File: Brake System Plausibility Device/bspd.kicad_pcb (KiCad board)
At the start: 2 copper layers, 87.9 x 41.3 mm, 29 parts, among them P1 MX150_16, SW1 RESET, U1 MCP604, U2 LM1117-5.0, U3 74LVC2G74, U4 74AUC2G00

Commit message: BSPD Layout Done
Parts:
- removed P1: MX150_16, UNCAMotorsports:MX150_16pin
- removed R12, R13: 1k, Resistors_SMD:R_0805_HandSoldering
- removed RV1: 5KW trim - 10k, Potentiometers:Potentiometer_Trimmer_Bourns_3296W
- removed RV2: Braking trim - 10k, Potentiometers:Potentiometer_Trimmer_Bourns_3296W
- added BR: BRAKE_SENSOR, Pin_Headers:Pin_Header_Straight_1x03_Pitch2.54mm, F.Cu at (133.0, 88.8)
- added B_TR: 5KW trim - 10k, Potentiometers:Potentiometer_Trimmer_Bourns_3296W, F.Cu at (123.3, 105.2)
- added C5: 1u, Capacitors_SMD:C_0805_HandSoldering, B.Cu at (116.2, 98.4)
- added C6: 1u, Capacitors_SMD:C_0805_HandSoldering, F.Cu at (131.4, 101.1)
- added C7: 1u, Capacitors_SMD:C_0805_HandSoldering, B.Cu at (128.8, 106.9)
- added I_SNS_1: CURRENT_SENSE_2, Pin_Headers:Pin_Header_Straight_1x03_Pitch2.54mm, F.Cu at (110.2, 88.9)
- added I_SNS_2: CURRENT_SENSE_1, Pin_Headers:Pin_Header_Straight_1x03_Pitch2.54mm, F.Cu at (110.2, 101.3)
- added I_TR: Braking trim - 10k, Potentiometers:Potentiometer_Trimmer_Bourns_3296W, F.Cu at (123.3, 89.7)
- added OUT: Q_QNOT_LATCHED, Pin_Headers:Pin_Header_Straight_1x02_Pitch2.54mm, F.Cu at (137.0, 106.4)
- added PWR: 12V_AND_GND, Pin_Headers:Pin_Header_Straight_1x02_Pitch2.54mm, F.Cu at (144.4, 98.3)
- added REF**: MountingHole_3.2mm_M3, Mounting_Holes:MountingHole_3.2mm_M3, F.Cu at (104.9, 104.8)
- added REF**: MountingHole_3.2mm_M3, Mounting_Holes:MountingHole_3.2mm_M3, F.Cu at (104.9, 90.4)
- added REF**: MountingHole_3.2mm_M3, Mounting_Holes:MountingHole_3.2mm_M3, F.Cu at (149.9, 104.8)
- added REF**: MountingHole_3.2mm_M3, Mounting_Holes:MountingHole_3.2mm_M3, F.Cu at (149.9, 90.4)
- C1, C2, D1, D2, D3, F1, R3, R4, R8, R9: moved to B.Cu
- C3: footprint Capacitors_ThroughHole:CP_Radial_D5.0mm_P2.00mm -> Capacitors_ThroughHole:CP_Radial_D6.3mm_P2.50mm
- R11: value 1k -> 10k
- SW1: value RESET -> SW_Push; footprint Buttons_Switches_ThroughHole:SW_PUSH_6mm -> Pin_Headers:Pin_Header_Straight_1x02_Pitch2.54mm
- U1: footprint Housings_SSOP:TSSOP-14_4.4x5mm_Pitch0.65mm -> SMD_Packages:SSOP-14
- U3: footprint Housings_SSOP:TSSOP-8_3x3mm_Pitch0.65mm -> Housings_SSOP:VSSOP-8_2.3x2mm_Pitch0.5mm
- moved R6 72.6 mm to (118.2, 94.1), turned to 180 degrees
- moved D2 69.5 mm to (125.1, 100.8), turned to 180 degrees
- moved C3 67.9 mm to (128.4, 94.7)
- moved U1 65.9 mm to (116.2, 98.5), turned to 270 degrees
- moved D1 61.3 mm to (120.2, 94.1), turned to 180 degrees
- moved C2 60.2 mm to (140.3, 91.7), turned to 270 degrees
- moved U2 58.4 mm to (139.6, 90.7), turned to 180 degrees
- moved U4 56.0 mm to (128.8, 105.7)
- moved SW1 55.5 mm to (142.0, 106.3), turned to 90 degrees
- moved C1 54.3 mm to (139.1, 88.4), turned to 180 degrees
- moved U3 46.5 mm to (128.0, 101.1), turned to 90 degrees
- moved C4 44.9 mm to (135.5, 97.5)
- moved R2 44.6 mm to (113.3, 104.0), turned to 270 degrees
- moved R7 42.8 mm to (122.9, 97.5), turned to 180 degrees
- moved R4 41.4 mm to (113.3, 105.4), turned to 270 degrees
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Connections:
- R11 pad 1: GND -> Net-(R11-Pad1)
- R11 pad 2: Net-(R11-Pad2) -> +5V
- SW1 pad 1: Net-(R11-Pad2) -> Net-(R11-Pad1)
- SW1 pad 2: +5V -> GND
- U3 pad 3: Net-(R13-Pad2) -> /BSPD_Latched_Output_NOT
- U3 pad 5: /TO_BTS6133 -> /BSPD_Latched_Output
- U4 pad 2: Net-(R11-Pad2) -> Net-(U4-Pad2)
- U4 pad 3: (no net) -> Net-(U4-Pad2)
- U4 pad 5: GND -> Net-(R11-Pad1)
- U4 pad 6: GND -> Net-(R11-Pad1)
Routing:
- net +5V: track 0.00 -> 45.6 mm, vias 0 -> 7
- net +12V: track 44.1 -> 5.53 mm, vias 0 -> 1
- net GND: track 0.00 -> 33.4 mm, vias 0 -> 6
- net /BSPD_Latched_Output: track 0.00 -> 25.5 mm, vias 0 -> 4
- net /BSPD: track 0.00 -> 20.8 mm, vias 0 -> 3
- net /Hard_Braking: track 0.00 -> 17.7 mm, vias 0 -> 4
- net Net-(R11-Pad1): track 0.00 -> 16.1 mm, vias 0 -> 2
- net Net-(R1-Pad2): track 0.00 -> 14.8 mm, vias 0 -> 2
- net Net-(C4-Pad1): track 0.00 -> 12.5 mm, vias 0 -> 2
- net Net-(C1-Pad1): track 0.00 -> 10.6 mm, vias 0 -> 1
- net /Current_R: track 0.00 -> 9.69 mm, vias 0 -> 2
- net Net-(RV2-Pad2): track 0.00 -> 9.45 mm
- net Net-(R10-Pad1): track 0.00 -> 8.46 mm
- net /BSPD_Latched_Output_NOT: track 0.00 -> 8.36 mm, vias 0 -> 1
- net Net-(D2-Pad2): track 0.00 -> 8.35 mm, vias 0 -> 2
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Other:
- board size 87.9 x 41.3 mm -> 52.1 x 21.5 mm
- net class Default: clearance 0.254 -> 0.1524
- rule trace_clearance: 0.254 -> 0.1524

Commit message: Fixed board error on BSPD
Track near via error corrected
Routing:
- net GND: vias 6 -> 5
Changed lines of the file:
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@@
 (kicad_pcb (version 4) (host pcbnew 4.0.6)
   (general
-    (links 0)
-    (no_connects 22)
-    (area 101.270999 86.792999 153.491001 108.406001)
+    (links 77)
+    (no_connects 0)
+    (area 95.392457 85.1786 159.369543 113.006972)
     (thickness 1.6)
     (drawings 12)
-    (tracks 255)
+    (tracks 254)
     (zones 0)
     (modules 38)
@@
     (pad_to_mask_clearance 0.2)
     (aux_axis_origin 0 0)
-    (visible_elements 7FFFFFFF)
+    (visible_elements 7FFFEFFF)
     (pcbplotparams
       (layerselection 0x00030_80000001)
@@
   (segment (start 128.762 102.854782) (end 128.928655 103.021437) (width 0.254) (layer F.Cu) (net 2))
   (segment (start 128.762 102.642) (end 128.762 102.854782) (width 0.254) (layer F.Cu) (net 2))
-  (via (at 129.413588 103.021437) (size 0.6858) (drill 0.3302) (layers F.Cu B.Cu) (net 2))
   (segment (start 128.928655 103.021437) (end 129.413588 103.021437) (width 0.254) (layer F.Cu) (net 2))
   (segment (start 129.413588 102.805613) (end 129.413588 103.021437) (width 0.254) (layer F.Cu) (net 2))

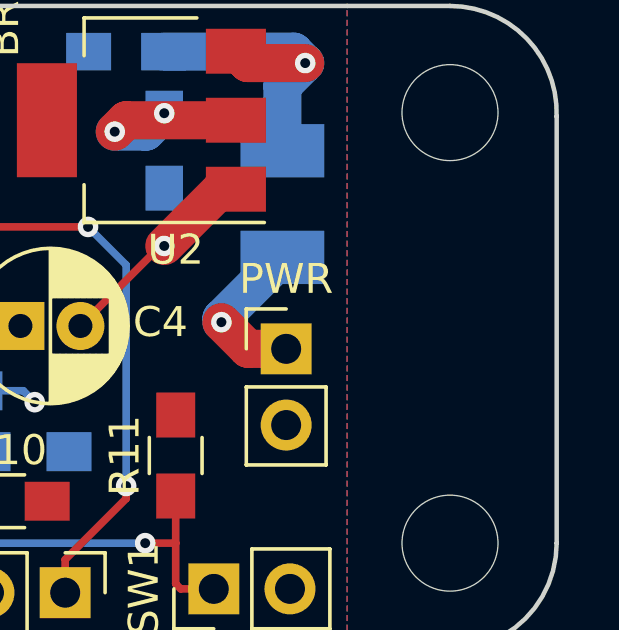
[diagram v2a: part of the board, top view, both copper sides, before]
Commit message: Reduce pour clearance to .1", add label
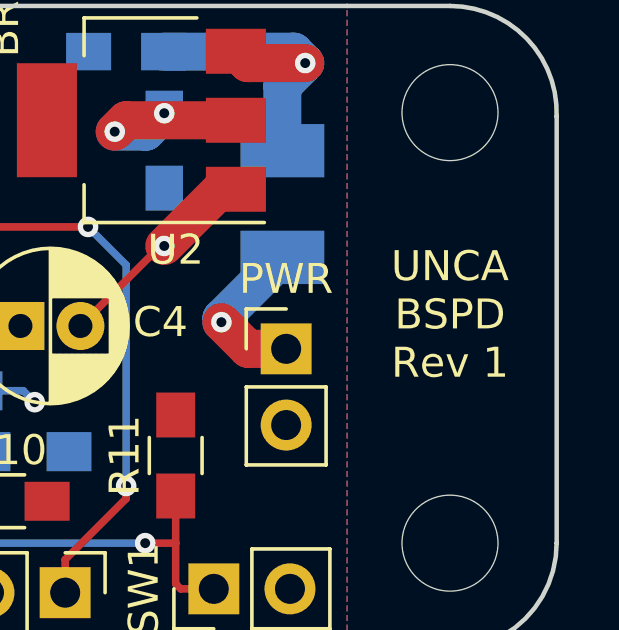
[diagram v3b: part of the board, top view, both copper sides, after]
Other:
- board text added: "UNCA BSPD Rev 1"
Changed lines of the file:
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@@
     (area 95.392457 85.1786 159.369543 113.006972)
     (thickness 1.6)
-    (drawings 12)
+    (drawings 13)
     (tracks 254)
     (zones 0)
@@
     (last_trace_width 0.254)
     (trace_clearance 0.1524)
-    (zone_clearance 0.508)
+    (zone_clearance 0.254)
     (zone_45_only no)
     (trace_min 0.1524)
@@
     (fp_circle (center 0 0) (end 3.45 0) (layer F.CrtYd) (width 0.05))
     (pad 1 np_thru_hole circle (at 0 0) (size 3.2 3.2) (drill 3.2) (layers *.Cu *.Mask))
+  )
+  (gr_text "UNCA\nBSPD\nRev 1" (at 149.86 97.155) (layer F.SilkS)
+    (effects (font (size 1 1) (thickness 0.2)))
   )
   (gr_arc (start 104.902 104.775) (end 104.902 108.331) (angle 90) (layer Edge.Cuts) (width 0.15))
@@
   (via (at 128.778 103.632) (size 0.6858) (drill 0.3302) (layers F.Cu B.Cu) (net 20))
   (zone (net 3) (net_name +5V) (layer F.Cu) (hatch edge 0.508)
-    (connect_pads (clearance 0.508))
+    (connect_pads (clearance 0.254))
     (min_thickness 0.254)
     (fill yes (arc_segments 16) (thermal_gap 0.508) (thermal_bridge_width 0.508))
@@
   )
   (zone (net 2) (net_name GND) (layer B.Cu) (hatch edge 0.508)
-    (connect_pads (clearance 0.508))
+    (connect_pads (clearance 0.254))
     (min_thickness 0.254)
     (fill yes (arc_segments 16) (thermal_gap 0.508) (thermal_bridge_width 0.508))
